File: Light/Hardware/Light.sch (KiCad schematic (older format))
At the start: 6 parts, among them J1 Conn_01x03, J2 Conn_01x03

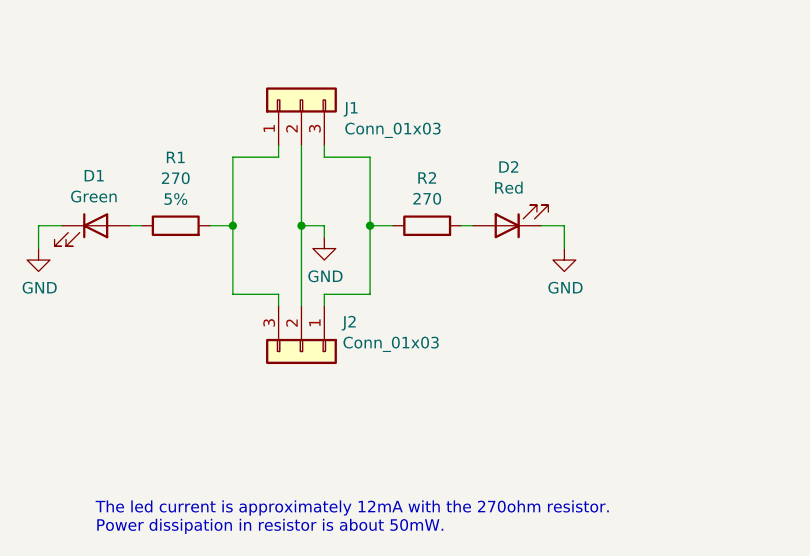
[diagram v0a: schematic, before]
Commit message: Added more component details to the 'light' schematic.
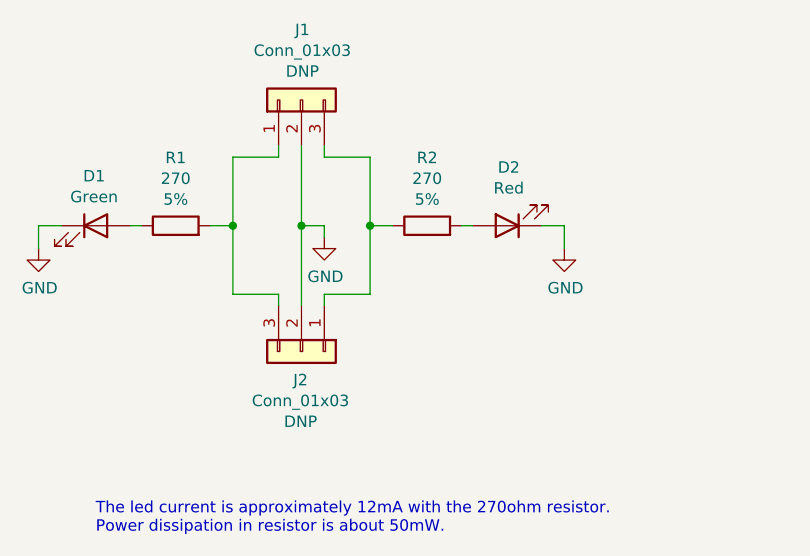
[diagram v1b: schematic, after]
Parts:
- J1, J2: Populate (none) -> DNP
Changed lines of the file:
@@
 U 1 1 620D6340
 P 4350 4100
-F 0 "J2" V 4222 4280 50  0000 L CNN
-F 1 "Conn_01x03" V 4313 4280 50  0000 L CNN
+F 0 "J2" V 4475 4096 50  0000 C CNN
+F 1 "Conn_01x03" V 4566 4096 50  0000 C CNN
 F 2 "Connector_PinHeader_2.54mm:PinHeader_1x03_P2.54mm_Horizontal" H 4350 4100 50  0001 C CNN
 F 3 "~" H 4350 4100 50  0001 C CNN
+F 4 "DNP" V 4657 4096 50  0000 C CNN "Populate"
 	1    4350 4100
 	0    1    1    0
@@
 U 1 1 620DA4B2
 P 4350 3000
-F 0 "J1" V 4314 2812 50  0000 R CNN
-F 1 "Conn_01x03" V 4223 2812 50  0000 R CNN
+F 0 "J1" V 4657 2996 50  0000 C CNN
+F 1 "Conn_01x03" V 4566 2996 50  0000 C CNN
 F 2 "Connector_PinHeader_2.54mm:PinHeader_1x03_P2.54mm_Horizontal" H 4350 3000 50  0001 C CNN
 F 3 "~" H 4350 3000 50  0001 C CNN
+F 4 "DNP" V 4475 2996 50  0000 C CNN "Populate"
 	1    4350 3000
 	0    -1   -1   0
@@
 U 1 1 620DED1F
 P 4900 3550
-F 0 "R2" V 5107 3550 50  0000 C CNN
-F 1 "270" V 5016 3550 50  0000 C CNN
+F 0 "R2" V 5197 3550 50  0000 C CNN
+F 1 "270" V 5106 3550 50  0000 C CNN
 F 2 "Resistor_SMD:R_1206_3216Metric_Pad1.30x1.75mm_HandSolder" V 4830 3550 50  0001 C CNN
 F 3 "~" H 4900 3550 50  0001 C CNN
-F 4 "5%" H 4900 3550 50  0001 C CNN "Value2"
+F 4 "5%" V 5015 3550 50  0000 C CNN "Value2"
 	1    4900 3550
 	0    -1   -1   0
